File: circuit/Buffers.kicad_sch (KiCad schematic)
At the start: 44 parts, among them J101 Pedal5_In, J102 Guitar_In, J103 Pedal6_In, J104 Amp_Out, J105 Pedal1_In, J106 Pedal7_In, J107 Pedal2_In, J108 Pedal8_In, J109 Pedal3_In, J110 Pedal4_In, U101 TL072, U102 TL072, U104 TL072, U105 TL072, U106 TL072

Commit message: Rebuilt bus and matrix.
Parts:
- renumbered C101 to C301, C102 to C302, C104 to C303, C105 to C304, C106 to C305, C108 to C306, C110 to C307, C111 to C308, C115 to C309, C116 to C310, C118 to C311, C119 to C312, C121 to C313, C122 to C314, C124 to C315, C125 to C316, C127 to C317, C128 to C318, C129 to C319, C130 to C320, J101 to J301, J102 to J302, J103 to J303, J104 to J304, J105 to J305, J106 to J306, J107 to J307, J108 to J308, J109 to J309, J110 to J310, R101 to R301, R102 to R302, R103 to R303, R104 to R304, R105 to R305, R106 to R306, R107 to R307, R108 to R308, R109 to R309, U102 to U11, U104 to U12, U106 to U13, U101 to U14, U105 to U15
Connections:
- net Guitar_Out renamed GUITAR_IN
- net Matrix_Out renamed MATRIX_OUT
- net Pedal1_Out renamed PEDAL_1_IN
- net Pedal2_Out renamed PEDAL_2_IN
- net Pedal3_Out renamed PEDAL_3_IN
- net Pedal4_Out renamed PEDAL_4_IN
- net Pedal5_Out renamed PEDAL_5_IN
- net Pedal6_Out renamed PEDAL_6_IN
- net Pedal7_Out renamed PEDAL_7_IN
- net Pedal8_Out renamed PEDAL_8_IN
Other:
- moved on the sheet: C306, C313, C314, C319, R303, R306, R307, R309

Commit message: Hopefully close to finished
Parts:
- J301, J302, J303, J304, J305, J306, J307, J308, J309, J310: footprint Connector_Wire:SolderWire-0.1sqmm_1x02_P3.6mm_D0.4mm_OD1mm -> Bay:Pedal_Jack
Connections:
- net MATRIX_OUT renamed MATRIX_OUT_PRE
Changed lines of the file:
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@@
 		)
 	)
-	(global_label "MATRIX_OUT"
+	(global_label "MATRIX_OUT_PRE"
 		(shape input)
 		(at 36.83 43.18 180)
@@
 			)
 		)
-		(property "Footprint" "Connector_Wire:SolderWire-0.1sqmm_1x02_P3.6mm_D0.4mm_OD1mm"
+		(property "Footprint" "Bay:Pedal_Jack"
 			(at 24.13 166.37 0)
 			(effects
@@
 			)
 		)
-		(property "Footprint" "Connector_Wire:SolderWire-0.1sqmm_1x02_P3.6mm_D0.4mm_OD1mm"
+		(property "Footprint" "Bay:Pedal_Jack"
 			(at 33.02 30.48 0)
 			(effects
@@
 			)
 		)
-		(property "Footprint" "Connector_Wire:SolderWire-0.1sqmm_1x02_P3.6mm_D0.4mm_OD1mm"
+		(property "Footprint" "Bay:Pedal_Jack"
 			(at 25.4 88.9 0)
 			(effects
@@
 			)
 		)
-		(property "Footprint" "Connector_Wire:SolderWire-0.1sqmm_1x02_P3.6mm_D0.4mm_OD1mm"
+		(property "Footprint" "Bay:Pedal_Jack"
 			(at 25.4 153.67 0)
 			(effects
@@
 			)
 		)
-		(property "Footprint" "Connector_Wire:SolderWire-0.1sqmm_1x02_P3.6mm_D0.4mm_OD1mm"
+		(property "Footprint" "Bay:Pedal_Jack"
 			(at 140.97 40.64 0)
 			(effects
@@
 			)
 		)
-		(property "Footprint" "Connector_Wire:SolderWire-0.1sqmm_1x02_P3.6mm_D0.4mm_OD1mm"
+		(property "Footprint" "Bay:Pedal_Jack"
 			(at 140.97 101.6 0)
 			(effects
@@
 			)
 		)
-		(property "Footprint" "Connector_Wire:SolderWire-0.1sqmm_1x02_P3.6mm_D0.4mm_OD1mm"
+		(property "Footprint" "Bay:Pedal_Jack"
 			(at 142.24 88.9 0)
 			(effects
@@
 			)
 		)
-		(property "Footprint" "Connector_Wire:SolderWire-0.1sqmm_1x02_P3.6mm_D0.4mm_OD1mm"
+		(property "Footprint" "Bay:Pedal_Jack"
 			(at 142.24 27.94 0)
 			(effects
@@
 			)
 		)
-		(property "Footprint" "Connector_Wire:SolderWire-0.1sqmm_1x02_P3.6mm_D0.4mm_OD1mm"
+		(property "Footprint" "Bay:Pedal_Jack"
 			(at 24.13 101.6 0)
 			(effects
@@
 			)
 		)
-		(property "Footprint" "Connector_Wire:SolderWire-0.1sqmm_1x02_P3.6mm_D0.4mm_OD1mm"
+		(property "Footprint" "Bay:Pedal_Jack"
 			(at 107.95 43.18 0)
 			(effects

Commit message: Created pdf and made minor readabilty changes.
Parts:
- C303, C304, C305, C306, C311, C312, C313, C314, C318, C319: value 1mF -> 1uF
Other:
- title: (none) -> ESP332 Guitar Patch Bay
- moved on the sheet: C301, C303, C306, C307, C310, C312, C314, C316, J301, J303, J306, J308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

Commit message: Rebuilt Matrix and added inhibit function.
Matrix was flawed, It now supports 8 FX loops (pedals) in any order. Or optionally none at all with a buffered bypass, or anywhere in between. The inhibit function will allow the option to press any loop foot switch an enable or disable it without reprogramming.
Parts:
- added C317, C318, C319, C320, C321, C322, C323, C324: 0.1uF, Capacitor_THT:C_Axial_L3.8mm_D2.6mm_P7.50mm_Horizontal, symbol Device:C_Small
- added C325, C326, C327, C328, C329, C330, C331, C332: 1uF, Capacitor_THT:C_Axial_L3.8mm_D2.6mm_P7.50mm_Horizontal, symbol Device:C_Small
- added J309: FX_S_1, Bay:Pedal_Jack, symbol Connector_Audio:AudioJack2
- added J310: FX_S_2, Bay:Pedal_Jack, symbol Connector_Audio:AudioJack2
- added J311: FX_S_3, Bay:Pedal_Jack, symbol Connector_Audio:AudioJack2
- added J312: FX_S_4, Bay:Pedal_Jack, symbol Connector_Audio:AudioJack2
- added J313: FX_S_5, Bay:Pedal_Jack, symbol Connector_Audio:AudioJack2
- added J314: FX_S_6, Bay:Pedal_Jack, symbol Connector_Audio:AudioJack2
- added J315: FX_S_7, Bay:Pedal_Jack, symbol Connector_Audio:AudioJack2
- added J316: FX_S_8, Bay:Pedal_Jack, symbol Connector_Audio:AudioJack2
- added R309, R310, R311, R312, R313, R314, R315, R316: 10k, Resistor_THT:R_Axial_DIN0204_L3.6mm_D1.6mm_P5.08mm_Horizontal, symbol Device:R_US
- added U304, U305, U306, U307: TL072, Package_DIP:CERDIP-8_W7.62mm_SideBrazed, symbol Bay:TL072
- J301: renamed from J307; value Pedal2_In -> FX_R_2
- J302: renamed from J310; value Pedal4_In -> FX_R_4
- J303: value Pedal6_In -> FX_R_56
- J304: renamed from J308; value Pedal8_In -> FX_R_8
- J305: value Pedal1_In -> FX_R_1
- J306: renamed from J309; value Pedal3_In -> FX_R_3
- J307: renamed from J301; value Pedal5_In -> FX_R_5
- J308: renamed from J306; value Pedal7_In -> FX_R_7
- renumbered C306 to C301, C314 to C302, C313 to C303, C319 to C304, C311 to C305, C318 to C306, C303 to C307, C312 to C308, C315 to C309, C320 to C310, C307 to C311, C316 to C312, C309 to C313, C317 to C314, C301 to C315, C310 to C316, C304 to C333, C308 to C334, C302 to C335, C305 to C336, J302 to J317, J304 to J318, R306 to R301, R307 to R302, R309 to R303, R303 to R304, R304 to R305, R308 to R306, R301 to R307, R305 to R308, R302 to R317, U12 to U11'301, U13 to U301, U14 to U302, U15 to U303, U11 to U308
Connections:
- net +15V: now also C321.2, C322.2, C323.2, C324.2, U304.8 (V+), U305.8 (V+), U306.8 (V+), U307.8 (V+)
- net -15V: now also C317.1, C318.1, C319.1, C320.1, U304.4 (V-), U305.4 (V-), U306.4 (V-), U307.4 (V-)
- net AGND: now also C317.2, C318.2, C319.2, C320.2, C321.1, C322.1, C323.1, C324.1, J309.S, J310.S, J311.S, J312.S, J313.S, J314.S, J315.S, J316.S
- net PEDAL_1_IN renamed FX_R_1
- net PEDAL_2_IN renamed FX_R_2
- net PEDAL_3_IN renamed FX_R_3
- net PEDAL_4_IN renamed FX_R_4
- net PEDAL_5_IN renamed FX_R_5
- net PEDAL_6_IN renamed FX_R_6
- net PEDAL_7_IN renamed FX_R_7
- net PEDAL_8_IN renamed FX_R_8
- new net: C325.1, J309.T
- new net: C325.2, R309.2
- new net: R311.1, U305.1 (1OUT), U305.2 (1-)
- new net: R312.1, U305.6 (2-), U305.7 (2OUT)
- new net: R315.1, U307.1 (1OUT), U307.2 (1-)
- new net: R316.1, U307.6 (2-), U307.7 (2OUT)
- new net: C328.1, J312.T
- new net: C328.2, R312.2
- new net: R310.1, U304.6 (2-), U304.7 (2OUT)
- new net: C326.2, R310.2
- new net: C331.1, J315.T
- new net: C327.1, J311.T
- new net: C332.2, R316.2
- new net: R309.1, U304.1 (1OUT), U304.2 (1-)
- new net: C329.1, J313.T
- new net: C329.2, R313.2
- new net: C326.1, J310.T
- new net: C330.1, J314.T
- new net: C330.2, R314.2
- new net: C332.1, J316.T
- new net: R313.1, U306.1 (1OUT), U306.2 (1-)
- new net: C327.2, R311.2
- new net: C331.2, R315.2
- new net: R314.1, U306.6 (2-), U306.7 (2OUT)
- new net FX_S_1: U304.3 (1+)
- new net FX_S_2: U304.5 (2+)
- new net FX_S_3: U305.3 (1+)
- new net FX_S_4: U305.5 (2+)
- new net FX_S_5: U306.3 (1+)
- new net FX_S_6: U306.5 (2+)
- new net FX_S_7: U307.3 (1+)
- new net FX_S_8: U307.5 (2+)
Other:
- moved on the sheet: C301, C302, C303, C304, C305, C306, C307, C308, C309, C310, C311, C312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

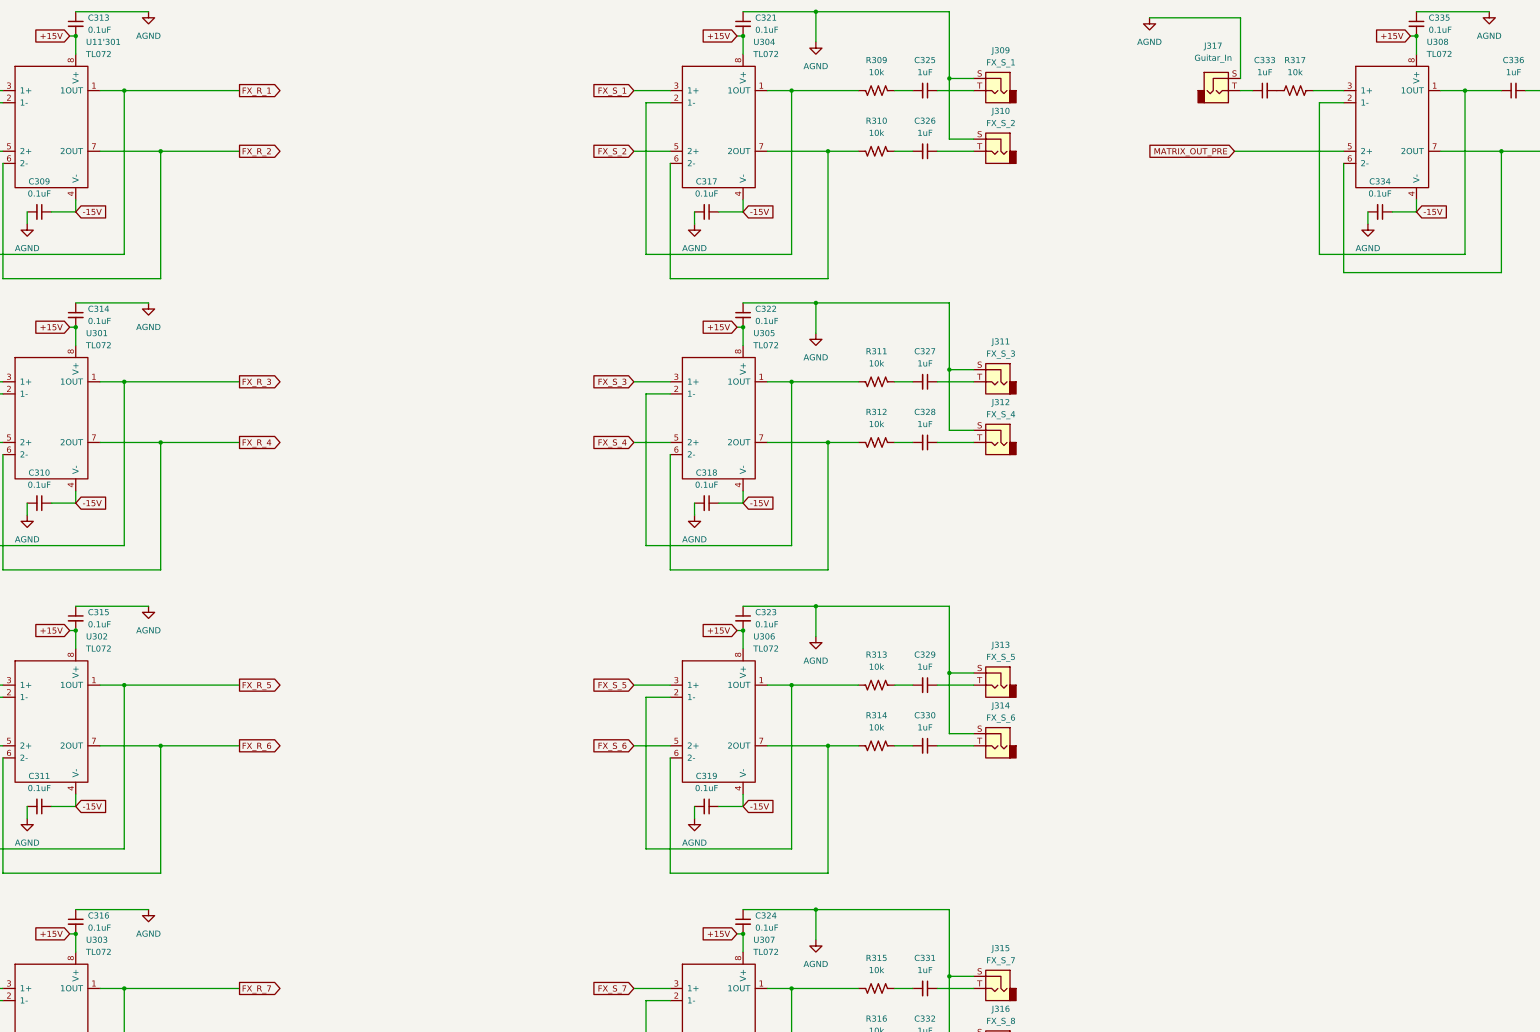
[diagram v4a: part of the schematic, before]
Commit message: Re-annotation of circuit, new PCB routing, updated PDF
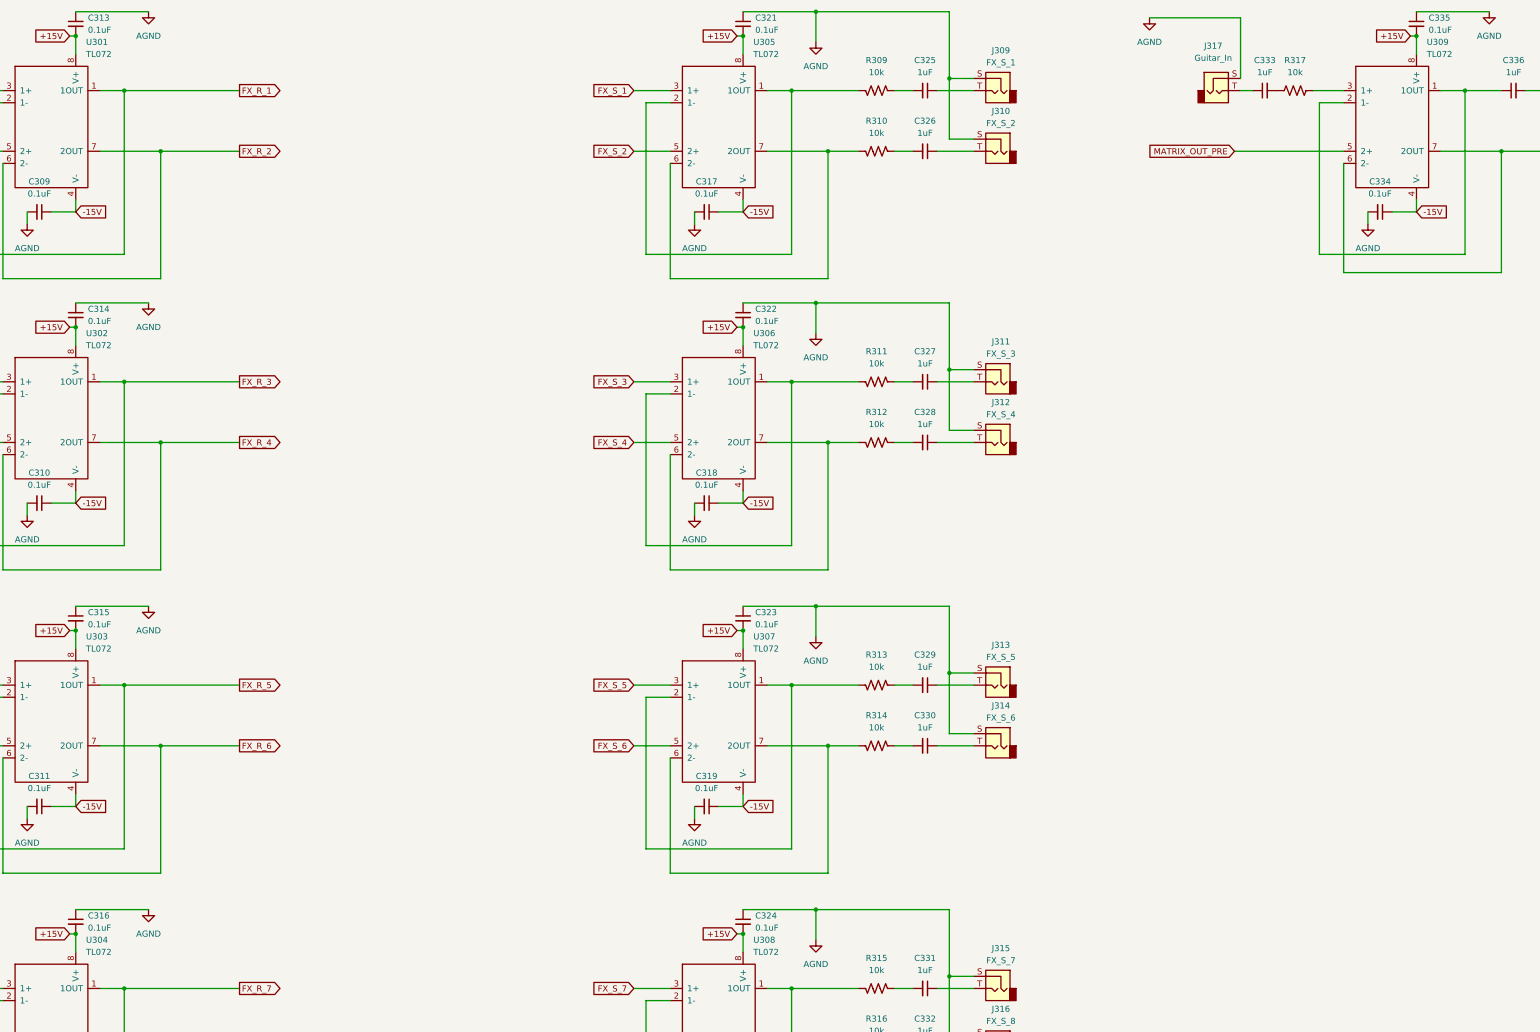
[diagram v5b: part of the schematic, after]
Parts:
- renumbered U11'301 to U301, U301 to U302, U302 to U303, U303 to U304, U304 to U305, U305 to U306, U306 to U307, U307 to U308, U308 to U309
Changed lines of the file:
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@@
 		(dnp no)
 		(fields_autoplaced yes)
-		(property "Reference" "U11'301"
-			(at 79.6133 22.87 0)
+		(property "Reference" "U301"
+			(at 79.6133 22.86 0)
 			(effects
 				(font
@@
 		)
 		(property "Value" "TL072"
-			(at 79.6133 25.41 0)
+			(at 79.6133 25.4 0)
 			(effects
 				(font
@@
 			(project "circuit"
 				(path "/420e3d7a-6c9a-4806-b4be-05d56aeb21de/91f6596b-9a37-4517-8aab-00555625375a"
-					(reference "U11'301")
+					(reference "U301")
 					(unit 1)
 				)
@@
 		(dnp no)
 		(fields_autoplaced yes)
-		(property "Reference" "U305"
+		(property "Reference" "U306"
 			(at 219.3133 83.83 0)
 			(effects
@@
 			(project "circuit"
 				(path "/420e3d7a-6c9a-4806-b4be-05d56aeb21de/91f6596b-9a37-4517-8aab-00555625375a"
-					(reference "U305")
+					(reference "U306")
 					(unit 1)
 				)
@@
 		(dnp no)
 		(fields_autoplaced yes)
-		(property "Reference" "U307"
+		(property "Reference" "U308"
 			(at 219.3133 210.83 0)
 			(effects
@@
 			(project "circuit"
 				(path "/420e3d7a-6c9a-4806-b4be-05d56aeb21de/91f6596b-9a37-4517-8aab-00555625375a"
-					(reference "U307")
+					(reference "U308")
 					(unit 1)
 				)
@@
 		(dnp no)
 		(fields_autoplaced yes)
-		(property "Reference" "U302"
+		(property "Reference" "U303"
 			(at 79.6133 147.33 0)
 			(effects
@@
 			(project "circuit"
 				(path "/420e3d7a-6c9a-4806-b4be-05d56aeb21de/91f6596b-9a37-4517-8aab-00555625375a"
-					(reference "U302")
+					(reference "U303")
 					(unit 1)
 				)
@@
 		(dnp no)
 		(fields_autoplaced yes)
-		(property "Reference" "U308"
+		(property "Reference" "U309"
 			(at 360.2833 22.86 0)
 			(effects
@@
 			(project "circuit"
 				(path "/420e3d7a-6c9a-4806-b4be-05d56aeb21de/91f6596b-9a37-4517-8aab-00555625375a"
-					(reference "U308")
+					(reference "U309")
 					(unit 1)
 				)
@@
 		(dnp no)
 		(fields_autoplaced yes)
-		(property "Reference" "U301"
+		(property "Reference" "U302"
 			(at 79.6133 83.83 0)
 			(effects
@@
 			(project "circuit"
 				(path "/420e3d7a-6c9a-4806-b4be-05d56aeb21de/91f6596b-9a37-4517-8aab-00555625375a"
-					(reference "U301")
+					(reference "U302")
 					(unit 1)
 				)
@@
 		(dnp no)
 		(fields_autoplaced yes)
-		(property "Reference" "U303"
+		(property "Reference" "U304"
 			(at 79.6133 210.83 0)
 			(effects
@@
 			(project "circuit"
 				(path "/420e3d7a-6c9a-4806-b4be-05d56aeb21de/91f6596b-9a37-4517-8aab-00555625375a"
-					(reference "U303")
+					(reference "U304")
 					(unit 1)
 				)
@@
 		(dnp no)
 		(fields_autoplaced yes)
-		(property "Reference" "U304"
+		(property "Reference" "U305"
 			(at 219.3133 22.87 0)
 			(effects
@@
 			(project "circuit"
 				(path "/420e3d7a-6c9a-4806-b4be-05d56aeb21de/91f6596b-9a37-4517-8aab-00555625375a"
-					(reference "U304")
+					(reference "U305")
 					(unit 1)
 				)
@@
 		(dnp no)
 		(fields_autoplaced yes)
-		(property "Reference" "U306"
+		(property "Reference" "U307"
 			(at 219.3133 147.33 0)
 			(effects
@@
 			(project "circuit"
 				(path "/420e3d7a-6c9a-4806-b4be-05d56aeb21de/91f6596b-9a37-4517-8aab-00555625375a"
-					(reference "U306")
+					(reference "U307")
 					(unit 1)
 				)

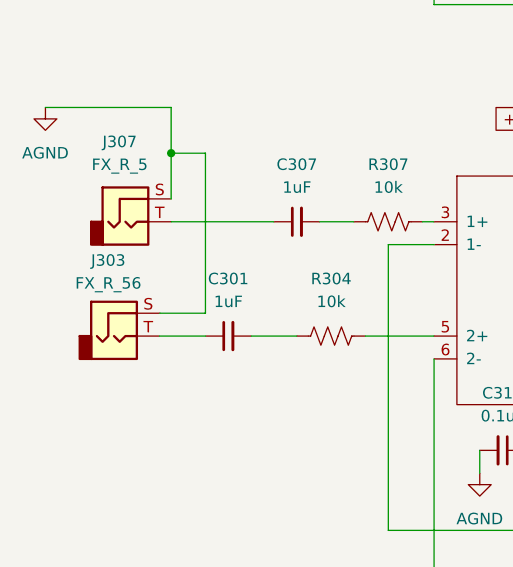
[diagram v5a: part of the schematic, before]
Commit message: Fine tuning of circuit
Added jumper to select voltage of display, changed 3.3V regulator from SMD to TO-220 to simplify DIY builds.
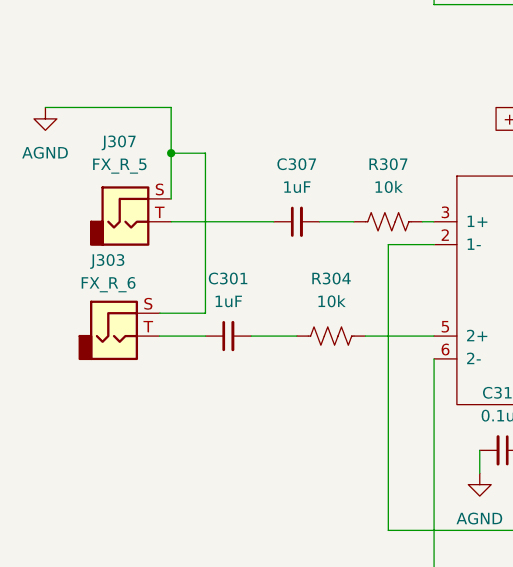
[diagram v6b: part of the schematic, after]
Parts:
- J303: value FX_R_56 -> FX_R_6
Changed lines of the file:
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@@
 			)
 		)
-		(property "Value" "FX_R_56"
+		(property "Value" "FX_R_6"
 			(at 26.035 164.32 0)
 			(effects

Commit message: Added ferrite beads and tweaked PCB
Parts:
- added L301, L302, L309, L310: 600R@100Mhz, WE-UKW:WE-UKW_74275010, symbol WE_UKW:WE-UKW_1SW_74275010
- C301, C302, C303, C304, C305, C306, C307, C308, C309, C310, C311, C312, C313, C314, C315, C316, C317, C318, C319, C320, C321, C322, C323, C324, C325, C326, C327, C328, C329, C330, C331, C332, C333, C334, C335, C336: footprint Capacitor_THT:C_Axial_L3.8mm_D2.6mm_P7.50mm_Horizontal -> Capacitor_THT:C_Disc_D3.0mm_W2.0mm_P2.50mm
- J301, J302, J303, J304, J305, J306, J307, J308, J309, J310, J311, J312, J313, J314, J315, J316, J317, J318: footprint Bay:Pedal_Jack -> Library:Jack
- R301, R302, R303, R304, R305, R306, R307, R308, R309, R310, R311, R312, R313, R314, R315, R316, R317: footprint Resistor_THT:R_Axial_DIN0204_L3.6mm_D1.6mm_P5.08mm_Horizontal -> Resistor_THT:R_Axial_DIN0207_L6.3mm_D2.5mm_P7.62mm_Horizontal
- U301, U302, U303, U304, U305, U306, U307, U308, U309: footprint Package_DIP:CERDIP-8_W7.62mm_SideBrazed -> Package_DIP:DIP-8_W7.62mm
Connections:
- net +15V: now also L301.1, L309.1; no longer C313.2, C314.2, C315.2, C316.2, C321.2, C322.2, C323.2, C324.2, C335.2, U301.8 (V+), U302.8 (V+), U303.8 (V+), U304.8 (V+), U305.8 (V+), U306.8 (V+), U307.8 (V+), U308.8 (V+), U309.8 (V+)
- net -15V: now also L302.2, L310.2; no longer C309.1, C310.1, C311.1, C312.1, C317.1, C318.1, C319.1, C320.1, C334.1, U301.4 (V-), U302.4 (V-), U303.4 (V-), U304.4 (V-), U305.4 (V-), U306.4 (V-), U307.4 (V-), U308.4 (V-), U309.4 (V-)
- new net: C317.1, C318.1, C319.1, C320.1, C334.1, L310.1, U305.4 (V-), U306.4 (V-), U307.4 (V-), U308.4 (V-), U309.4 (V-)
- new net: C321.2, C322.2, C323.2, C324.2, C335.2, L309.2, U305.8 (V+), U306.8 (V+), U307.8 (V+), U308.8 (V+), U309.8 (V+)
- new net +15V_F: C313.2, C314.2, C315.2, C316.2, L301.2, U301.8 (V+), U302.8 (V+), U303.8 (V+), U304.8 (V+)
- new net _15V_F: C309.1, C310.1, C311.1, C312.1, L302.1, U301.4 (V-), U302.4 (V-), U303.4 (V-), U304.4 (V-)
